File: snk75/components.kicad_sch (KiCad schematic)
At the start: 37 parts, among them J2 USB_C_Receptacle_USB2.0, Q1 AO3400A, U3 USBLC6-2SC6, U4 XC6206P332MR, U5 SGM2007-3.3XN5/TR

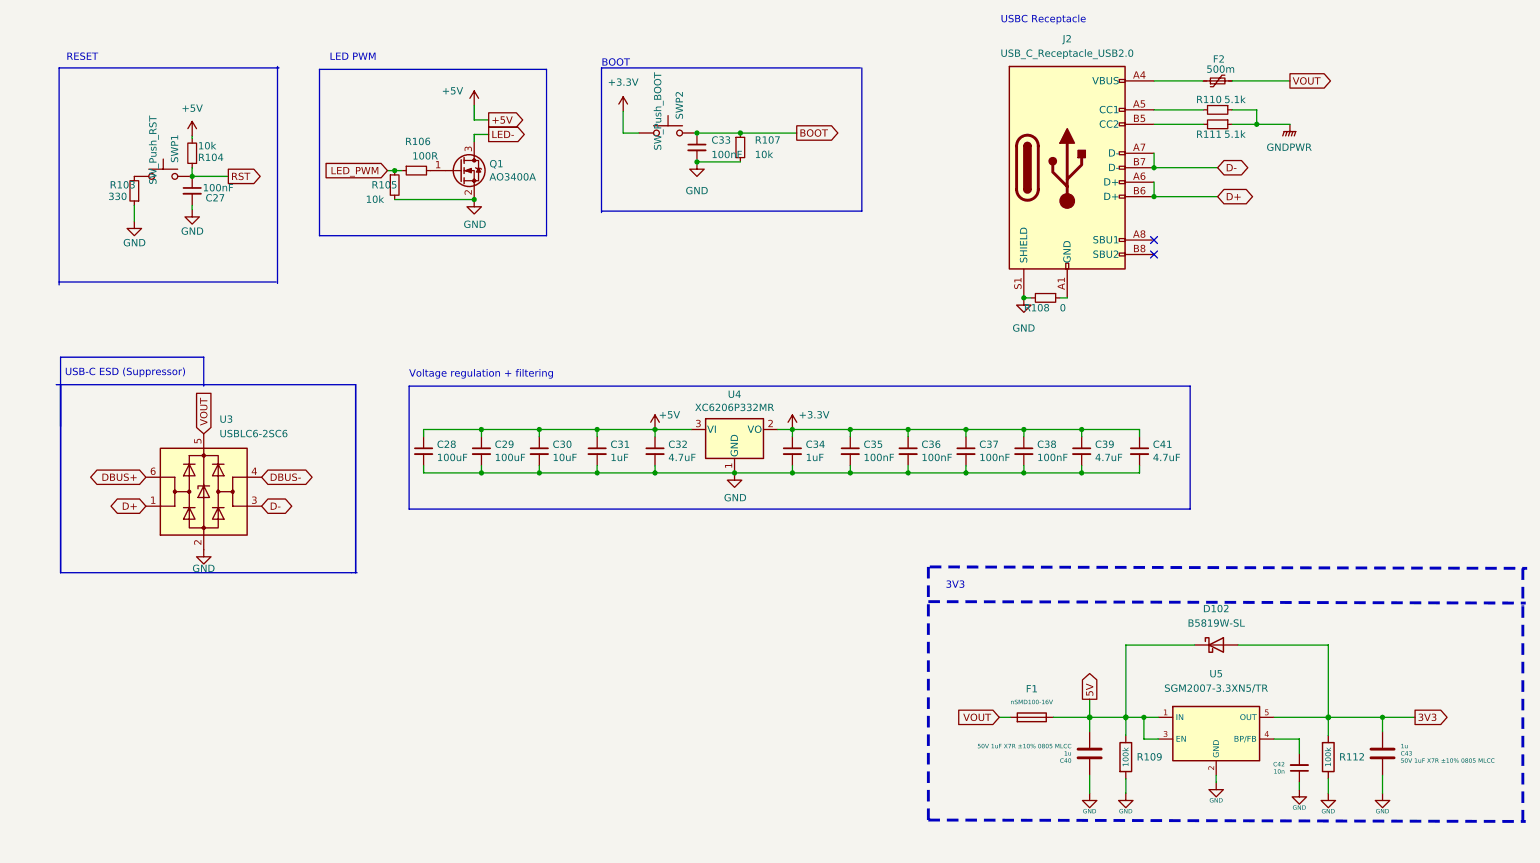
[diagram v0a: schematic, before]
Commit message: added components on board and began routing
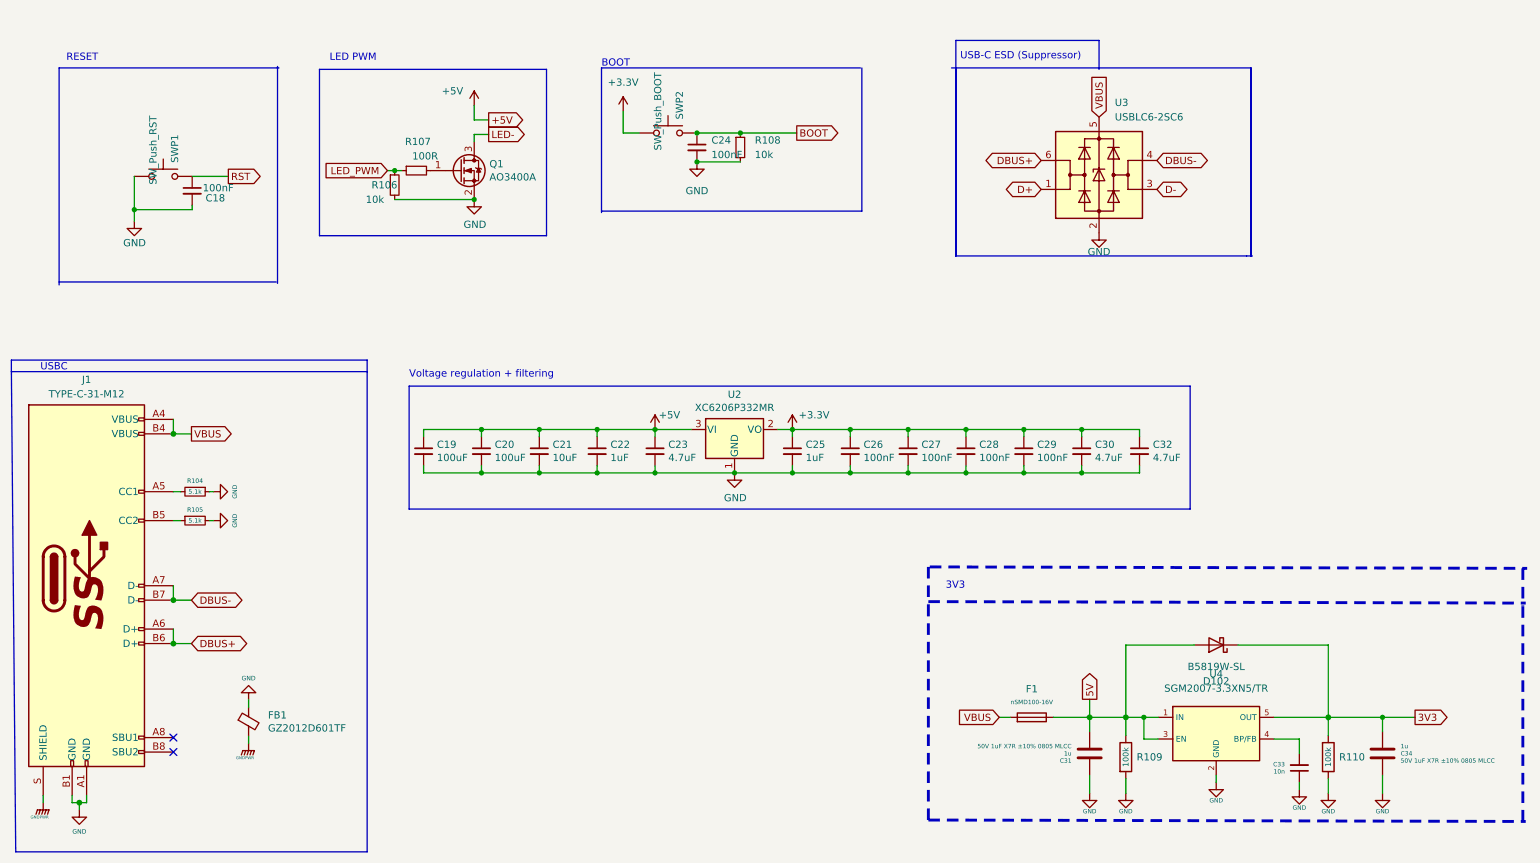
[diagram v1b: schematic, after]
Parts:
- removed F2: 500m, Fuse:Fuse_1206_3216Metric, symbol Device:Polyfuse_Small
- removed J2: USB_C_Receptacle_USB2.0, Connector_USB:USB_C_Receptacle_HRO_TYPE-C-31-M-12, symbol Connector:USB_C_Receptacle_USB2.0
- removed R103: 330, Resistor_SMD:R_0402_1005Metric, symbol Device:R_Small
- removed R108: 0, Resistor_SMD:R_0402_1005Metric, symbol Device:R_Small
- removed R110, R111: 5.1k, Resistor_SMD:R_0402_1005Metric, symbol Device:R_Small
- added FB1: GZ2012D601TF, Inductor_SMD:L_0805_2012Metric, symbol Device:Ferrite_Bead_Small
- added J1: TYPE-C-31-M12, acheron_Connectors:TYPE-C-31-M-12, symbol acheronSymbols:USB_C_16_pin
- added R105: 5.1k, Resistor_SMD:R_0402_1005Metric, symbol Device:R_Small
- F1: footprint Fuse:Fuse_1206_3216Metric -> Fuse:Fuse_1206_3216Metric_Pad1.42x1.75mm_HandSolder
- R104: value 10k -> 5.1k; Manufacturer (none) -> Uniroyal; Manufacturer Part Number (none) -> 0402WGF5101TCE; Package (none) -> R0402; Specification (none) -> ±1% 1/16W Thick Film Resistors 50V 0805; Vendor Part Number (none) -> LCSC C25905
- R110: renamed from R112; footprint Resistor_SMD:R_0805_2012Metric -> Resistor_SMD:R_0402_1005Metric
- renumbered C27 to C18, C28 to C19, C29 to C20, C30 to C21, C31 to C22, C32 to C23, C33 to C24, C34 to C25, C35 to C26, C36 to C27, C37 to C28, C38 to C29, C39 to C30, C40 to C31, C41 to C32, C42 to C33, C43 to C34, R105 to R106, R106 to R107, R107 to R108, U4 to U2, U5 to U4
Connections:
- net +5V: no longer R104.2
- net 3V3: now also D102.1 (K); no longer D102.2 (A)
- net 5V: now also D102.2 (A); no longer D102.1 (K)
- net DBUS+: now also J1.A6 (D+), J1.B6 (D+)
- net DBUS-: now also J1.A7 (D-), J1.B7 (D-)
- net GND: now also R104.1, SWP1.1, FB1.1, J1.A1 (GND), J1.B1 (GND), R105.2
- net GNDPWR: now also FB1.2, J1.S (SHIELD)
- net RST: no longer R104.1
- net VOUT renamed VBUS
- net VBUS: now also J1.A4 (VBUS), J1.B4 (VBUS)
- new net: J1.B5 (CC2), R105.1
- new net: J1.A5 (CC1), R104.2
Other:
- note added: "USBC"
- note removed: "USBC Receptacle"
- moved on the sheet: D102, U3

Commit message: WIP: Removed wrong path, gonna rebuild with better designed path
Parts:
- C19, C20: footprint Capacitor_Tantalum_SMD:CP_EIA-3528-21_Kemet-B -> Capacitor_SMD:C_0402_1005Metric
- C21: footprint Capacitor_Tantalum_SMD:CP_EIA-3216-18_Kemet-A -> Capacitor_SMD:C_0402_1005Metric
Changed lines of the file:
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@@
       (effects (font (size 1.27 1.27)) (justify left))
     )
-    (property "Footprint" "Capacitor_Tantalum_SMD:CP_EIA-3216-18_Kemet-A" (id 2) (at 109.474 92.71 0)
+    (property "Footprint" "Capacitor_SMD:C_0402_1005Metric" (id 2) (at 109.474 92.71 0)
       (effects (font (size 1.27 1.27)) hide)
     )
@@
       (effects (font (size 1.27 1.27)) (justify left))
     )
-    (property "Footprint" "Capacitor_Tantalum_SMD:CP_EIA-3528-21_Kemet-B" (id 2) (at 89.154 92.71 0)
+    (property "Footprint" "Capacitor_SMD:C_0402_1005Metric" (id 2) (at 89.154 92.71 0)
       (effects (font (size 1.27 1.27)) hide)
     )
@@
       (effects (font (size 1.27 1.27)) (justify left))
     )
-    (property "Footprint" "Capacitor_Tantalum_SMD:CP_EIA-3528-21_Kemet-B" (id 2) (at 99.314 92.71 0)
-      (effects (font (size 1.27 1.27)) hide)
-    )
+    (property "Footprint" "Capacitor_SMD:C_0402_1005Metric" (id 2) (at 99.314 92.71 0)
+      (effects (font (size 1.27 1.27)) hide)
+    )

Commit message: WIP routes
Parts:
- removed C19, C20: 100uF, Capacitor_SMD:C_0402_1005Metric, symbol Device:C_Small
- removed C21: 10uF, Capacitor_SMD:C_0402_1005Metric, symbol Device:C_Small
- removed C22: 1uF, Capacitor_SMD:C_0402_1005Metric, symbol Device:C_Small
- removed C23, C32: 4.7uF, Capacitor_SMD:C_0402_1005Metric, symbol Device:C_Small
- removed U2: XC6206P332MR, Package_TO_SOT_SMD:SOT-23_Handsoldering, symbol isometria-75-pcb-iso-rescue:XC6206PxxxMR-Regulator_Linear-kicad-keyboard-parts
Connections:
- net 3V3 is gone; now on net +3V3: C34.2, D102.1 (K), R110.2, U4.5 (OUT)

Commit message: Nearly make all paths
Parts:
- added C29: 4.7uF, Capacitor_SMD:C_0402_1005Metric, symbol Device:C_Small
- C18: JLCPCB BOM (none) -> 1; LCSC (none) -> C1525; LCSC Part (none) -> C1525; LCSC Part Number (none) -> C1525
- C19: renamed from C24; JLCPCB BOM (none) -> 1; LCSC (none) -> C1525; LCSC Part (none) -> C1525; LCSC Part Number (none) -> C1525
- C20: renamed from C25; JLCPCB BOM (none) -> 1; LCSC Part (none) -> C52923; LCSC Part Number (none) -> C52923
- C21: renamed from C31; value 1u -> 1uF; JLCPCB BOM (none) -> 1; LCSC (none) -> C52923; LCSC Part (none) -> C215803; LCSC Part Number (none) -> C215803
- C22: renamed from C26; value 100nF -> 10nF; JLCPCB BOM (none) -> 1; LCSC Part (none) -> C1525; LCSC Part Number (none) -> C1525
- C23: renamed from C27; JLCPCB BOM (none) -> 1; LCSC Part (none) -> C1525; LCSC Part Number (none) -> C1525
- C24: renamed from C28; JLCPCB BOM (none) -> 1; LCSC Part (none) -> C1525; LCSC Part Number (none) -> C1525
- C25: renamed from C33; value 10n -> 10nF; JLCPCB BOM (none) -> 1; LCSC (none) -> C15195; LCSC Part (none) -> C15195; LCSC Part Number (none) -> C15195
- C26: renamed from C29; JLCPCB BOM (none) -> 1; LCSC Part (none) -> C1525; LCSC Part Number (none) -> C1525
- C27: renamed from C30; JLCPCB BOM (none) -> 1; LCSC Part (none) -> C23733; LCSC Part Number (none) -> C23733
- C28: renamed from C34; value 1u -> 1uF; JLCPCB BOM (none) -> 1; LCSC (none) -> C52923; LCSC Part (none) -> C215803; LCSC Part Number (none) -> C215803
- D102: JLCPCB BOM (none) -> 1; LCSC (none) -> C8598; LCSC Part (none) -> C8598; LCSC Part Number (none) -> C8598
- F1: JLCPCB BOM (none) -> 1; LCSC (none) -> C70082; LCSC Part (none) -> C70082; LCSC Part Number (none) -> C70082
- FB1: JLCPCB BOM (none) -> 1; LCSC (none) -> C1017; LCSC Part (none) -> C1017; LCSC Part Number (none) -> C1017
- J1: JLCPCB BOM (none) -> 1; LCSC (none) -> C165948; LCSC Part (none) -> C165948; LCSC Part Number (none) -> C165948
- Q1: JLCPCB BOM (none) -> 1; LCSC C20917 -> C347475; LCSC Part (none) -> C347475; LCSC Part Number (none) -> C347475
- R102: renamed from R104; JLCPCB BOM (none) -> 1; LCSC (none) -> C25905; LCSC Part (none) -> C25905; LCSC Part Number (none) -> C25905
- R103: renamed from R105; JLCPCB BOM (none) -> 1; LCSC (none) -> C25905; LCSC Part (none) -> C25905; LCSC Part Number (none) -> C25905
- R104: renamed from R106; JLCPCB BOM (none) -> 1; LCSC C25744 -> C269701; LCSC Part (none) -> C269701; LCSC Part Number (none) -> C269701
- R105: renamed from R107; JLCPCB BOM (none) -> 1; LCSC Part (none) -> C25076; LCSC Part Number (none) -> C25076
- R106: renamed from R108; JLCPCB BOM (none) -> 1; LCSC (none) -> C269701; LCSC Part (none) -> C269701; LCSC Part Number (none) -> C269701
- R107: renamed from R109; JLCPCB BOM (none) -> 1; LCSC (none) -> C149504; LCSC Part (none) -> C149504; LCSC Part Number (none) -> C149504
- R108: renamed from R110; JLCPCB BOM (none) -> 1; LCSC (none) -> C149504; LCSC Part (none) -> C149504; LCSC Part Number (none) -> C149504
- SWP1, SWP2: footprint Button_Switch_SMD:SW_MEC_5GSH9 -> Button_Switch_SMD:SW_SPST_SKQG_WithStem; JLCPCB BOM (none) -> 1; LCSC (none) -> C318886; LCSC Part (none) -> C318886; LCSC Part Number (none) -> C318886
- U2: renamed from U3; JLCPCB BOM (none) -> 1; LCSC (none) -> C7519; LCSC Part (none) -> C7519; LCSC Part Number (none) -> C7519
- U3: renamed from U4; JLCPCB BOM (none) -> 1; LCSC (none) -> C193687; LCSC Part (none) -> C193687; LCSC Part Number (none) -> C193687
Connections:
- net 5V is gone; now on net +5V: C21.1, D102.2 (A), F1.1, R107.1, U3.1 (IN), U3.3 (EN)
- net +3V3: now also C29.1
- net GND: now also C29.2
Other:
- moved on the sheet: C20, C21, C22, C23, C24, C25, C26, C27, C28, D102, F1, R107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
